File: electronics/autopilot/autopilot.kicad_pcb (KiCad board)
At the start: 2 copper layers, 70.4 x 68.8 mm, 30 parts, among them J1 SERVO, J10 MPPT_I2C, J11 Debug, J12 5V IN, J13 Vbatt, J2 SERVO, J3 SERVO, J4 SERVO, J5 ESC, J6 GSM_MODULE, J7 IBUS, J8 5V IN, J9 IMU, SW1 ARM, U1 Pico, U2 SIM28ML, U3 NRF24L01_Breakout, U4 74HC244

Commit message: autopilot rework
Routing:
- net GND: track 103.0 -> 343.0 mm, vias 10 -> 4
- net /GPS_RST: track 65.8 -> 72.6 mm
- net /GSM_RX: track 40.4 -> 42.8 mm
- net +3.3V: track 170.8 -> 168.8 mm, vias 6 -> 4
- net +5V: track 146.6 -> 148.3 mm
- net /PWM_SERVO2: track 27.3 -> 25.9 mm
- net Net-(R3-Pad2): track 13.3 -> 14.4 mm
- net /ESC: track 8.80 -> 7.86 mm
- net /PWM_SERVO3: track 25.3 -> 24.4 mm
- net /SCK: track 13.8 -> 13.0 mm, vias 2 -> 0
- net /PWM_SERVO1: track 27.1 -> 26.4 mm
- net /PWM_SERVO4: track 23.9 -> 23.2 mm
- net /PWM_ESC: track 29.0 -> 28.8 mm, vias 2 -> 1
- net /MOSI: vias 1 -> 0
- removed copper zone on B.Cu, net GND
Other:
- outline, holes or cut-outs redrawn

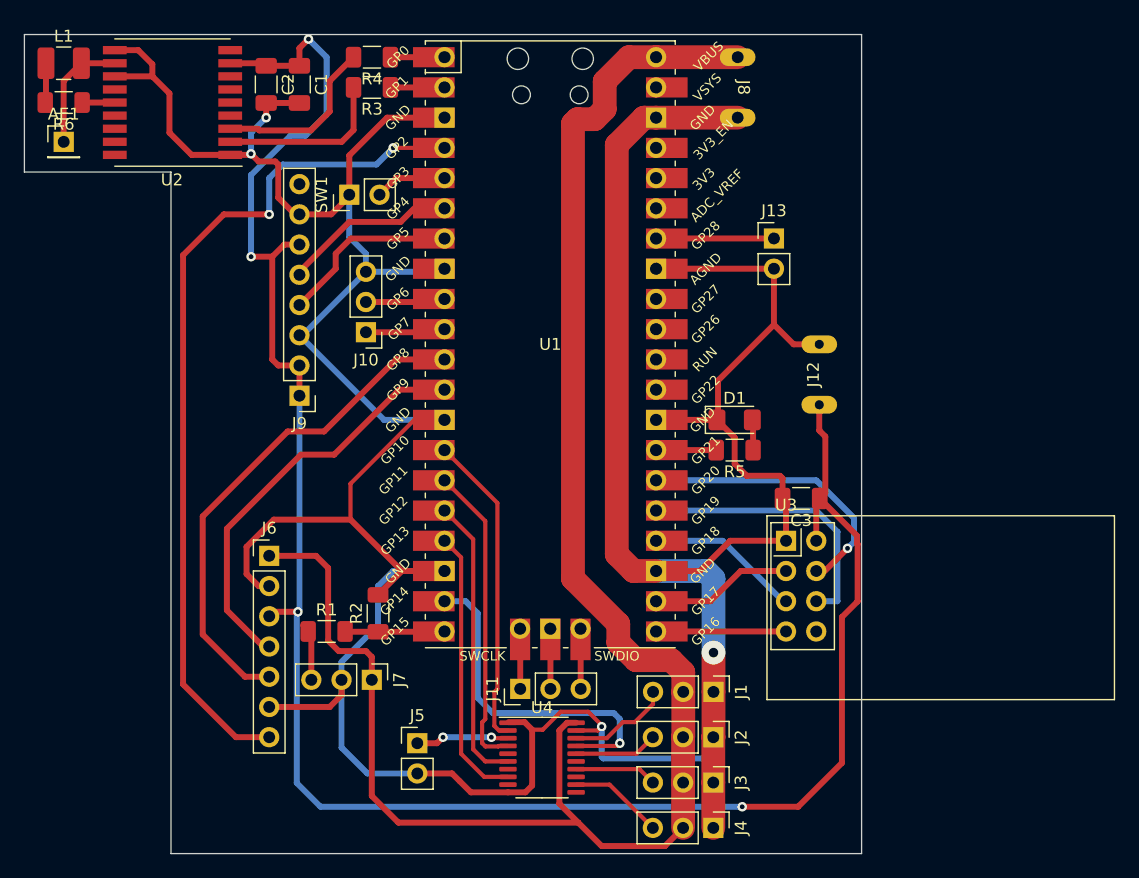
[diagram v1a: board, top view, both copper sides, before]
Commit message: autopilot buffer footprint fixed
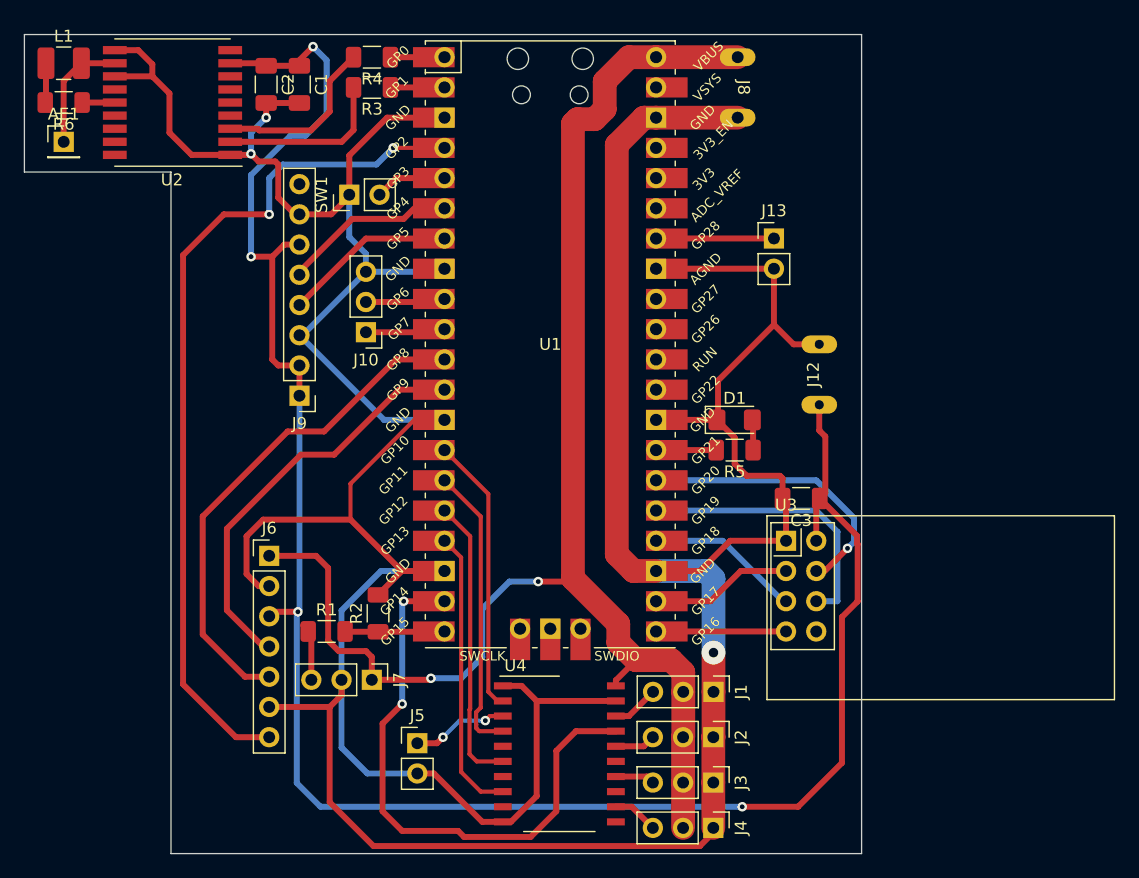
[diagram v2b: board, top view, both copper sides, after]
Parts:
- removed J11: Debug, Connector_PinHeader_2.54mm:PinHeader_1x03_P2.54mm_Vertical
- J12: value 5V IN -> 3.3V IN
- U4: footprint Package_SO:HTSSOP-20-1EP_4.4x6.5mm_P0.65mm_EP2.85x4mm -> Package_SO:SO-20_12.8x7.5mm_P1.27mm
- moved U4 1.49 mm to (140.2, 135.4)
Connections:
- net /GPS_RST renamed /GMS_RST
- U1 pad 41: Net-(J11-Pad1) -> unconnected-(U1-Pad41)
- U1 pad 42: Net-(J11-Pad2) -> unconnected-(U1-Pad42)
- U1 pad 43: Net-(J11-Pad3) -> unconnected-(U1-Pad43)
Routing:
- net GND: track 343.0 -> 377.0 mm, vias 4 -> 3
- net +5V: track 148.3 -> 125.6 mm, vias 0 -> 2
- net /PWM_ESC: track 28.8 -> 49.0 mm, vias 1 -> 2
- net Net-(J11-Pad3): track 5.06 -> 0.00 mm
- net Net-(J11-Pad2): track 5.06 -> 0.00 mm
- net Net-(J11-Pad1): track 5.06 -> 0.00 mm
- net /SERVO1: track 8.67 -> 3.97 mm
- net /SERVO4: track 7.96 -> 3.85 mm
- net /SERVO3: track 6.92 -> 3.32 mm
- net /SERVO2: track 7.02 -> 3.42 mm
- net /PWM_SERVO1: track 26.4 -> 23.4 mm
- net /PWM_SERVO2: track 25.9 -> 24.6 mm
- net +3.3V: track 168.8 -> 167.6 mm
- net /PWM_SERVO4: track 23.2 -> 24.2 mm
- net /IMU_I2C_SCL: track 15.3 -> 14.5 mm

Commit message: small fixes
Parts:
- removed AE1: Antenna, Connector_PinHeader_2.54mm:PinHeader_1x01_P2.54mm_Vertical
- added J11: Antena, Connector_Coaxial:U.FL_Molex_MCRF_73412-0110_Vertical, F.Cu at (98.6, 84.2)
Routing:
- net GND: track 377.0 -> 392.9 mm
- net Net-(L1-Pad2): track 10.0 -> 8.89 mm
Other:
- outline, holes or cut-outs redrawn
